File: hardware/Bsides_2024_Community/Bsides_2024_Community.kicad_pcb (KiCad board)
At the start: 2 copper layers, 169.6 x 159.5 mm, 45 parts, among them J1 Add_On, J2 Battery, J3 Battery, J4 OLED, J5 Conn_01x05, J6 Conn_01x05, P1 USB_C_Plug_USB2.0, Q1 DMG3415U-7, SW1 ON, SW2 RESET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

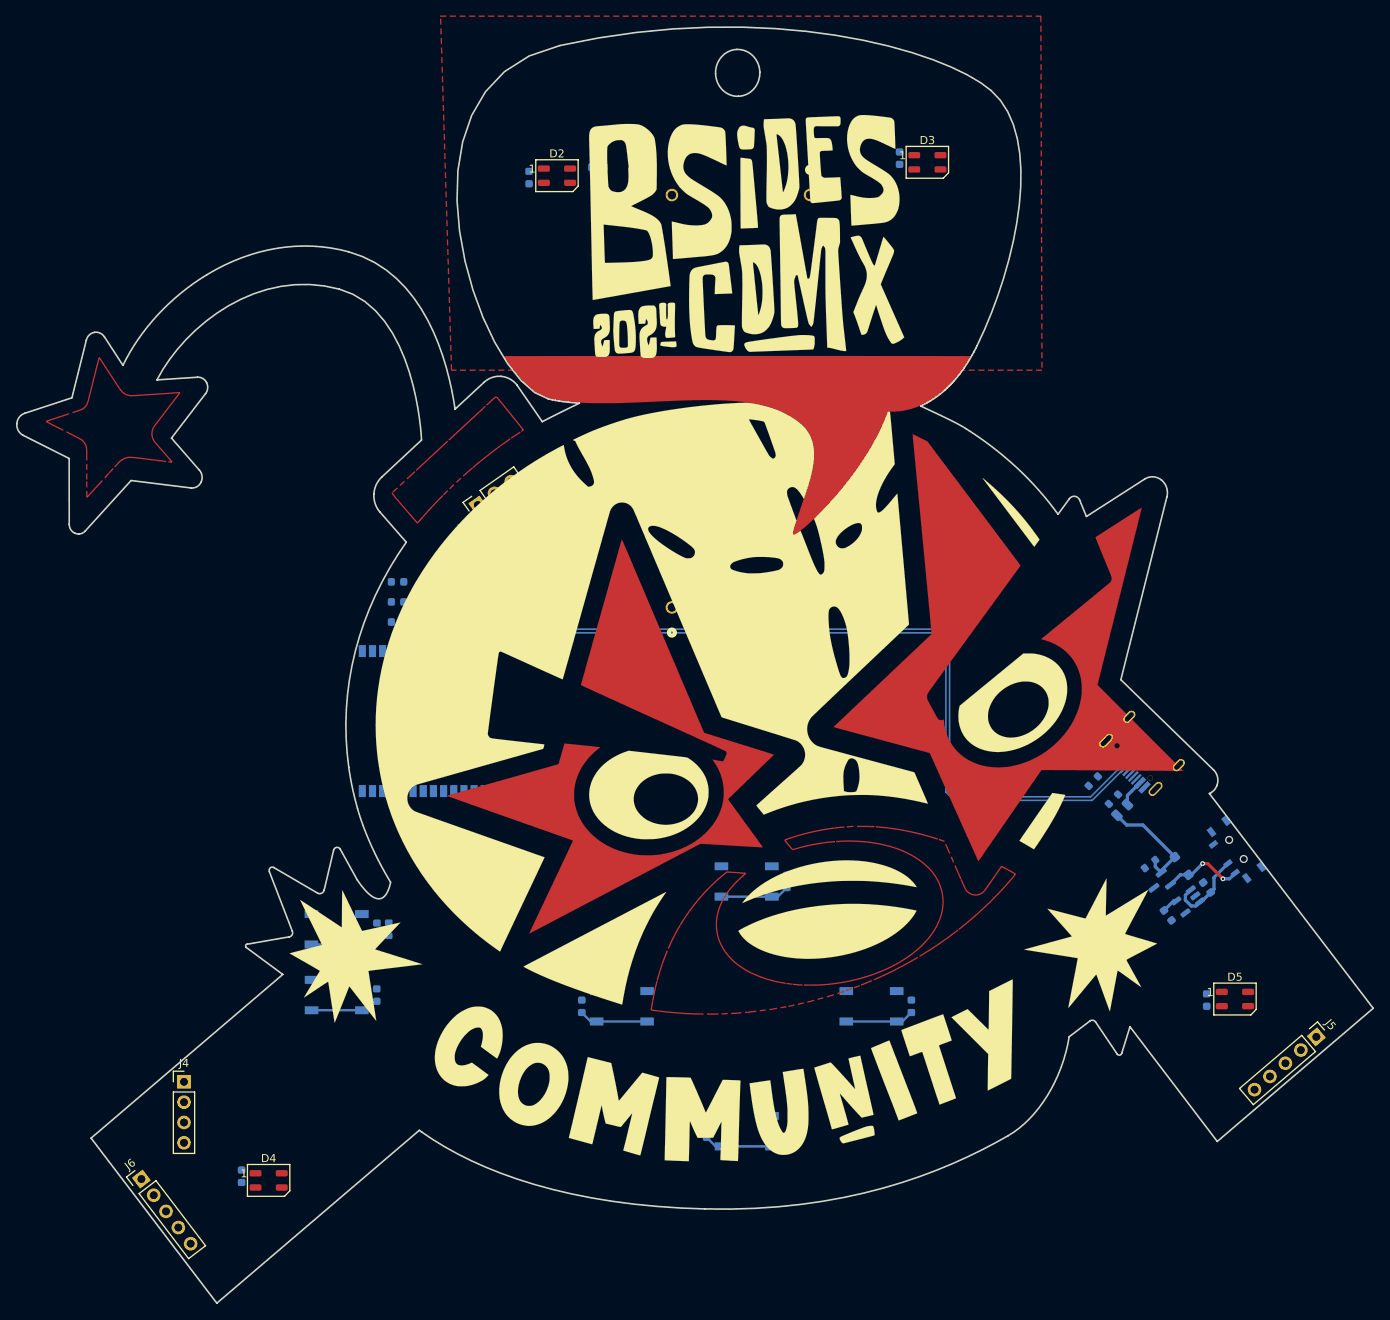
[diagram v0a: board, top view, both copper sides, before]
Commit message: Revert "Merge branch 'main' of https://github.com/ElectronicCats/badge-bsides-cdmx-2024"
This reverts commit 844f9cf1141b02d246949023f3a5d84c3d1d6870, reversing
changes made to df45190e2e7c4c17babbd6f5b24a18277498f0c6.
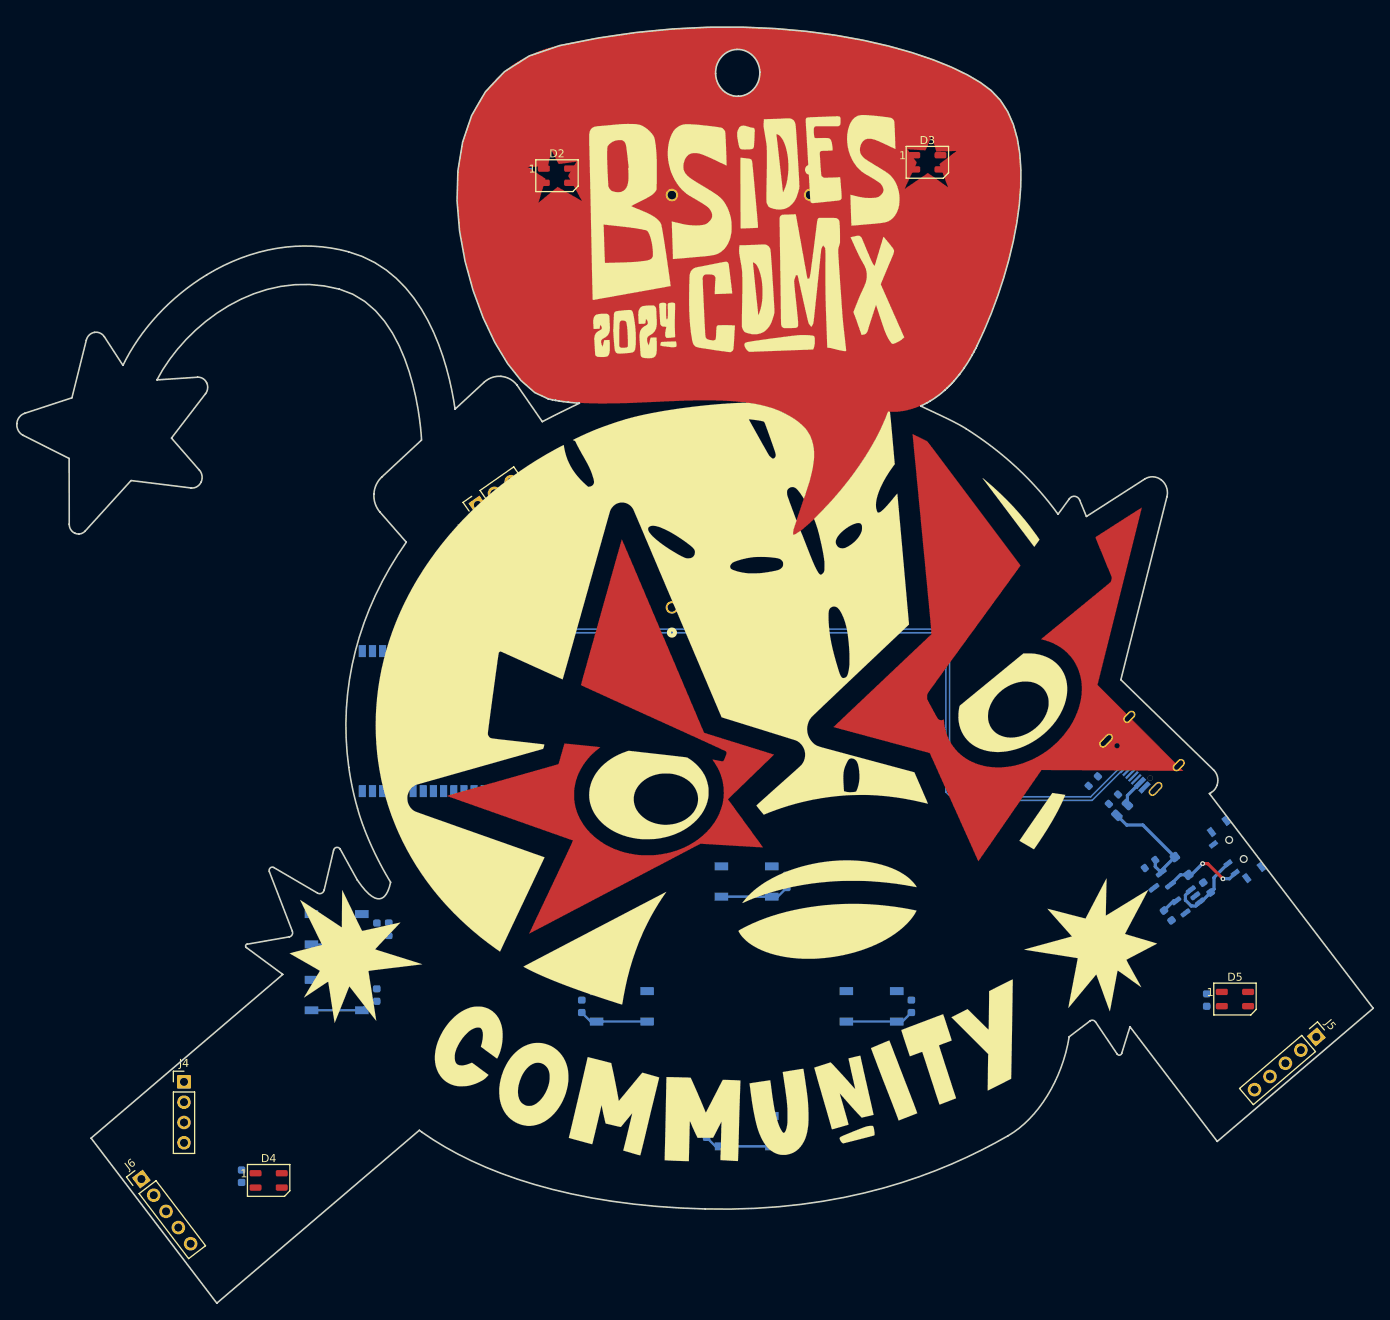
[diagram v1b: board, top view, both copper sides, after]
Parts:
- removed C13: 1uF, Capacitor_SMD:C_0603_1608Metric
- removed C14, C15: 10uF, Capacitor_SMD:C_0603_1608Metric
- J1: value Add_On -> Conn_02x03_Odd_Even
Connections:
- C1 pad 1: VBUS -> Net-(SW1-B)
- C12 pad 2: /VOUT -> +3V3
- C2 pad 1: Net-(D1-A) -> +3V3
- C5 pad 2: /VOUT -> +3V3
- C6 pad 2: /VOUT -> +3V3
- C7 pad 2: /VOUT -> +3V3
- D1 pad 2: Net-(D1-A) -> VBUS
- D2 pad 1: /VOUT -> +3V3
- D3 pad 1: /VOUT -> +3V3
- D4 pad 1: /VOUT -> +3V3
- D5 pad 1: /VOUT -> +3V3
- J1 pad 1: /VOUT -> unconnected-(J1-Pin_1-Pad1)
- J1 pad 2: GND -> unconnected-(J1-Pin_2-Pad2)
- J1 pad 3: /SDA -> unconnected-(J1-Pin_3-Pad3)
- J1 pad 4: /SCL -> unconnected-(J1-Pin_4-Pad4)
- J4 pad 1: /VOUT -> +3V3
- Q1 pad 1: Net-(D1-A) -> VBUS
- R1 pad 2: /VOUT -> +3V3
- R2 pad 1: Net-(D1-A) -> VBUS
- R5 pad 2: /VOUT -> +3V3
- SW1 pad 2: /VOUT -> Net-(SW1-B)
- U1 pad 2: /VOUT -> +3V3
- U2 pad 1: VBUS -> Net-(SW1-B)
- U2 pad 3: VBUS -> Net-(SW1-B)
- U2 pad 5: Net-(D1-A) -> +3V3
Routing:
- net VBUS: track 24.2 -> 14.0 mm
- net Net-(SW1-B): track 0.00 -> 10.3 mm
- net Net-(D1-A): track 2.04 -> 0.00 mm
- net +3V3: track 0.00 -> 2.04 mm
- removed copper zone on F.Cu, net (none)
- removed copper zone on F.Cu, net GND

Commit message: feat(Hw): Update PCB
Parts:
- added C13: 1uF, Capacitor_SMD:C_0603_1608Metric, B.Cu at (99.0, 90.5)
- added C14: 10uF, Capacitor_SMD:C_0603_1608Metric, B.Cu at (99.0, 93.0)
- added C15: 10uF, Capacitor_SMD:C_0603_1608Metric, B.Cu at (99.0, 95.5)
- J1: value Conn_02x03_Odd_Even -> Add_On
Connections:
- C1 pad 1: Net-(SW1-B) -> VBUS
- C12 pad 2: +3V3 -> /VOUT
- C2 pad 1: +3V3 -> Net-(D1-A)
- C5 pad 2: +3V3 -> /VOUT
- C6 pad 2: +3V3 -> /VOUT
- C7 pad 2: +3V3 -> /VOUT
- D1 pad 2: VBUS -> Net-(D1-A)
- D2 pad 1: +3V3 -> /VOUT
- D3 pad 1: +3V3 -> /VOUT
- D4 pad 1: +3V3 -> /VOUT
- D5 pad 1: +3V3 -> /VOUT
- J1 pad 1: unconnected-(J1-Pin_1-Pad1) -> /VOUT
- J1 pad 2: unconnected-(J1-Pin_2-Pad2) -> GND
- J1 pad 3: unconnected-(J1-Pin_3-Pad3) -> /SDA
- J1 pad 4: unconnected-(J1-Pin_4-Pad4) -> /SCL
- J4 pad 1: +3V3 -> /VOUT
- Q1 pad 1: VBUS -> Net-(D1-A)
- R1 pad 2: +3V3 -> /VOUT
- R2 pad 1: VBUS -> Net-(D1-A)
- R5 pad 2: +3V3 -> /VOUT
- SW1 pad 2: Net-(SW1-B) -> /VOUT
- U1 pad 2: +3V3 -> /VOUT
- U2 pad 1: Net-(SW1-B) -> VBUS
- U2 pad 3: Net-(SW1-B) -> VBUS
- U2 pad 5: +3V3 -> Net-(D1-A)
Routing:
- net VBUS: track 14.0 -> 24.2 mm
- net Net-(SW1-B): track 10.3 -> 0.00 mm
- net Net-(D1-A): track 0.00 -> 2.04 mm
- net +3V3: track 2.04 -> 0.00 mm
- added copper zone on F.Cu, net (none)
- added copper zone on F.Cu, net GND
